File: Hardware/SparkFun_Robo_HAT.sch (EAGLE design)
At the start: 128 parts, among them J1 RASPBERRYPI-40-PIN-GPIO_PTH_R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, J11 EXT MTR PWR, J18 ISP, J2 CORTEX_DEBUGPTH, J20 USB C, J7 EXT SERVO PWR, J8 EXT 5V PWR, Q1 310mA/60V/1.6Ω, Q23 20V/0.2A/8MHz/1.2Ω/1Vth, Q24 20V/0.2A/8MHz/1.2Ω/1Vth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

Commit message: sch cleanup and drc stuff in brd
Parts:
- removed J2: CORTEX_DEBUGPTH, Pete_Connectors_Retired:CORTEX_DEBUGPTH
- removed TP18, TP19, TP24: TEST-POINTTP_15TH_THRU, SparkFun-Connectors:TEST-POINTTP_15TH_THRU
- added J23: CORTEX_JTAG_DEBUG_PTH, SparkFun-Connectors:CORTEX_JTAG_DEBUG_PTH
- added TP4, TP6: TEST-POINTTP_15TH_THRU, SparkFun-Connectors:TEST-POINTTP_15TH_THRU
- added TP9: TEST-POINT3, SparkFun-Connectors:TEST-POINT3
- TP5: value 1.8V -> TEST-POINTTP_15TH_THRU; device SparkFun-Connectors:TEST-POINT3 -> SparkFun-Connectors:TEST-POINTTP_15TH_THRU
- renumbered TP11 to TP7, TP12 to TP8
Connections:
- net !MTR_RST: now also J23.!RESET; no longer J2.NRESET
- net 1.8V: now also TP9.1; no longer TP5.1
- net 3.3V: now also J23.VCC; no longer J2.VCC
- net GND: now also J23.GND@3, J23.GND@5, J23.GNDDTCT, J23.KEY; no longer J2.GND@3, J2.GND@5, J2.GNDDTCT, J2.KEY
- net P3.2: now also J23.SWDIO/TMS; no longer J2.SWDIO/TMS
- net P3.3: now also J23.SWDCLK/TCK; no longer J2.SWDCLK/TCK
- net PI-5V: now also TP6.1; no longer TP24.1
- net SCL_3.3V: now also TP4.1; no longer TP18.1
- net SDA_3.3V: now also TP5.1; no longer TP19.1
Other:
- note added: "Servo Controller based on a design by Mike Hord Serial Controlled Motor Driver based on designs by Marshall Taylor, Alex Wende ICM-20948 based on a design by Owen Lyke ATTINY84 Encoder based on a design by Nathan Seidle"
- moved on the sheet: C12, C13, C14, C24, C25, J10, J19, J22, J3, J4, J5, U5

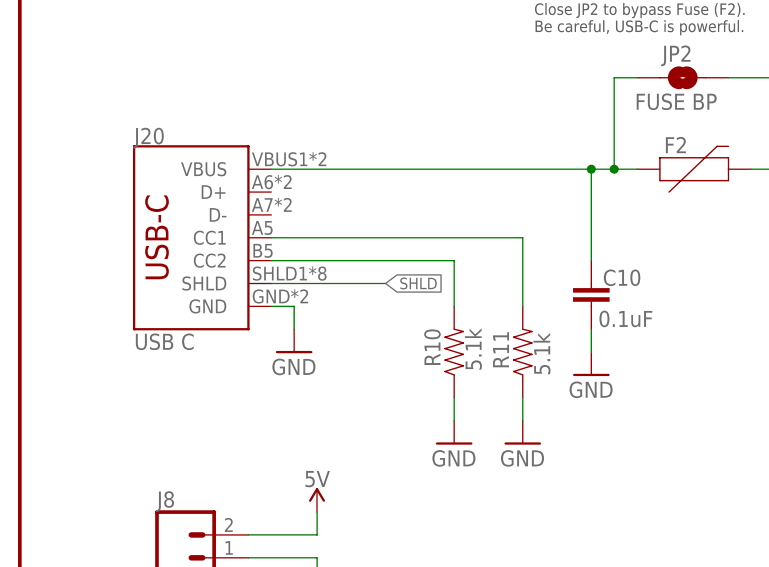
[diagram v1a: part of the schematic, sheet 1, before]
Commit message: removed USB C Shield polygon
to let more GND flow under connector up to Pi Header.
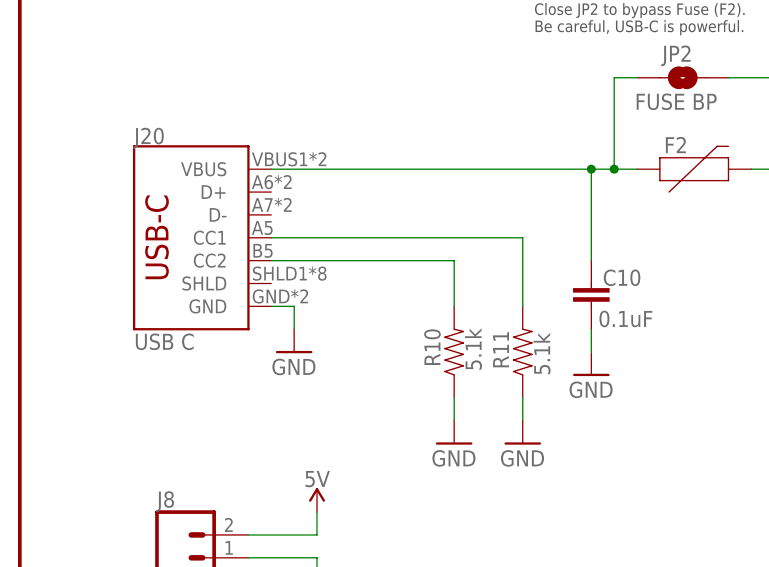
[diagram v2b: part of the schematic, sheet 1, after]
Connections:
- removed net SHLD: J20.SHLD
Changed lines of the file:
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@@
-</segment>
-</net>
-<net name="SHLD" class="0">
-<segment>
-<wire x1="27.94" y1="223.52" x2="40.64" y2="223.52" width="0.1524" layer="91"/>
-<label x="40.64" y="223.52" size="1.27" layer="95" font="vector" xref="yes"/>
-<pinref part="J20" gate="J1" pin="SHLD"/>
 </segment>
 </net>

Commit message: Engineer 1st run of checklist
added measures and SS path, cleaned up sch a bit more.
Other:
- note added: "VCC RANGE: 5V only (via USB or J8)"
- note removed: "VCC RANGE: 5V only (via USB or J21)"
- moved on the sheet: C11, C16, C2, C23, C26, C27, J18, JP13, R22, R37, R38, R39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

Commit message: post design review changes
-moved TP P3.0 programming pSoc onto grid
-Added pulldown resistor on Config line on PSoc
-Added trestric under pSoC to avoid GND pad nubbins.
-Added pullup resistors to SDA_OUT and SCL_OUT, as consistent with original serial controlled motor driver.
-Switched over to design block for pi header and slots. re-routed some stuff to make it work.
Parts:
- removed FD2, FD3, FD4: FIDUCIALUFIDUCIAL, SparkFun-Aesthetics:FIDUCIALUFIDUCIAL
- removed J1: RASPBERRYPI-40-PIN-GPIO_PTH_REFERENCE, SparkFun-Connectors:RASPBERRYPI-40-PIN-GPIO_PTH_REFERENCE
- added FD5, FD7, FD8: FIDUCIALUFIDUCIAL, SparkFun-Aesthetics:FIDUCIALUFIDUCIAL
- added H10, H11, H12, H9: STAND-OFFTIGHT, SparkFun-Hardware:STAND-OFFTIGHT
- added J2: RASPBERRYPI-40-PIN-GPIO_PTH_NO_SHROUD, SparkFun-Connectors:RASPBERRYPI-40-PIN-GPIO_PTH_NO_SHROUD
- added R12, R3, R6: 5.1k, SparkFun-Resistors:5.1KOHM5.1KOHM-0603-1/10W-1%
- renumbered FD1 to FD6
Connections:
- new net CONFIG_OUT: R6.2, U6G4.P3.0
- new net SCL_OUT: R12.1, U6G5.P4.0
- new net SDA_OUT: R3.1, U6G5.P4.1
- net !ENC_INT: now also J2.GP4; no longer J1.GP4
- net 3.3V: now also J2.3.3V, R12.2, R3.2; no longer J1.3.3V
- net GND: now also J2.GND, R6.1; no longer J1.GND
- net IMU_INT_3.3V: now also J2.CE1; no longer J1.CE1
- net N$20: now also J2.5V; no longer J1.5V
- net SCL_3.3V: now also J2.SCL; no longer J1.SCL
- net SDA_3.3V: now also J2.SDA; no longer J1.SDA
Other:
- moved on the sheet: C17, C18, C19, C20, C21, C22, C23, R25, R26, U6G1, U6G3, U6G4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

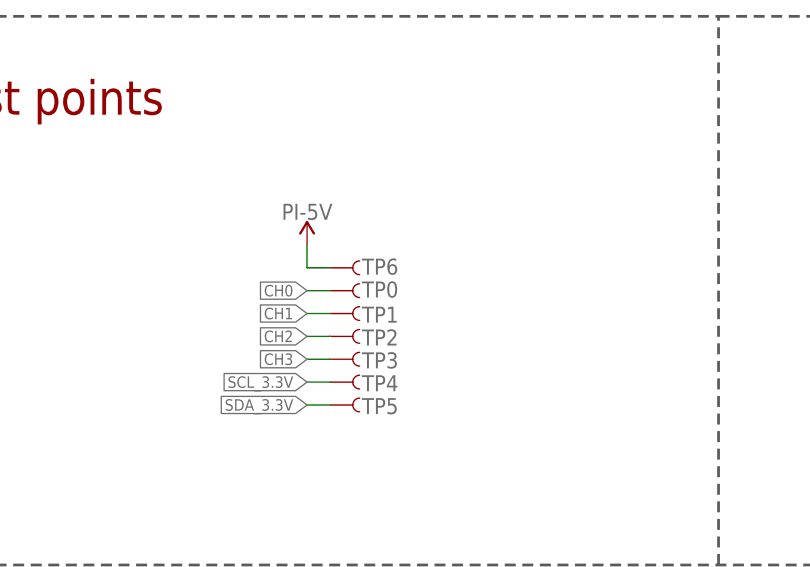
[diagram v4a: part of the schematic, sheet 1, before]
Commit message: post double-check changes - ready for proto v01
-moved TP6 to SMT pad style and on grid
-updated tran-14386 (ideal diode) to have polarity mark outside package
-nudged vias to avoid silk labels
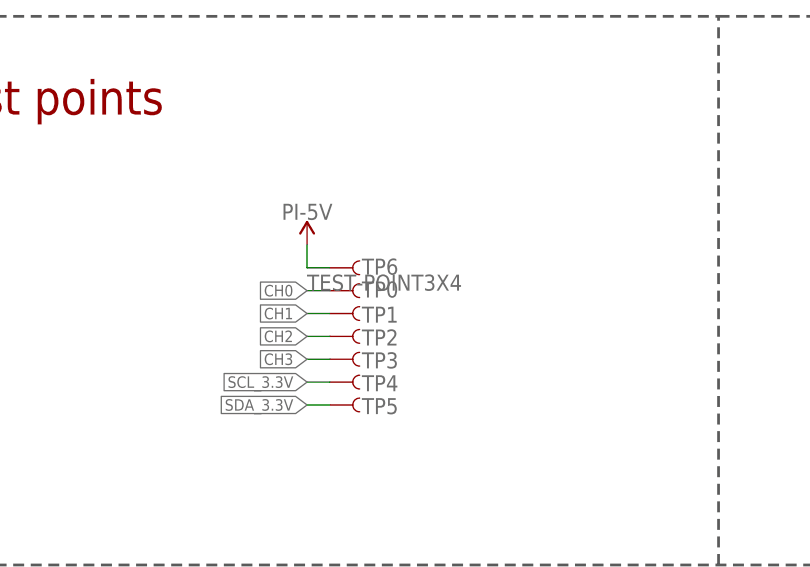
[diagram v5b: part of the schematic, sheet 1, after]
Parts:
- Q23, Q24, Q27, Q28: device SparkFun-DiscreteSemi:MOSFET-NCH-RE1C002UN -> SparkFun-DiscreteSemi:MOSFET-NCH-RE1C00UNTL
- TP6: value TEST-POINTTP_15TH_THRU -> TEST-POINT3X4; device SparkFun-Connectors:TEST-POINTTP_15TH_THRU -> SparkFun-Connectors:TEST-POINT3X4

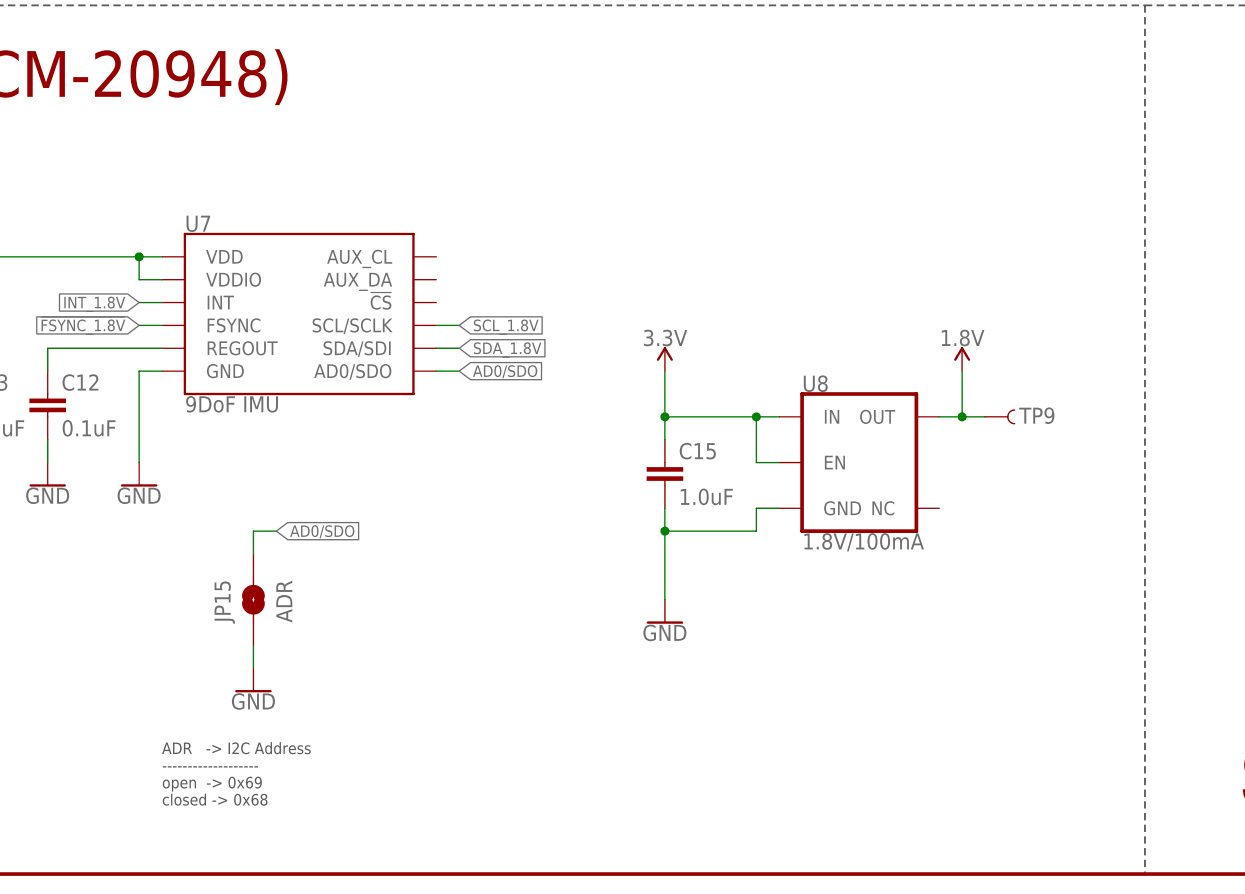
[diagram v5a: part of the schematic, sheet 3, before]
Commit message: Connected IMU CS pin to 1.8V, Added IMU ADR PU 2.2K resistor
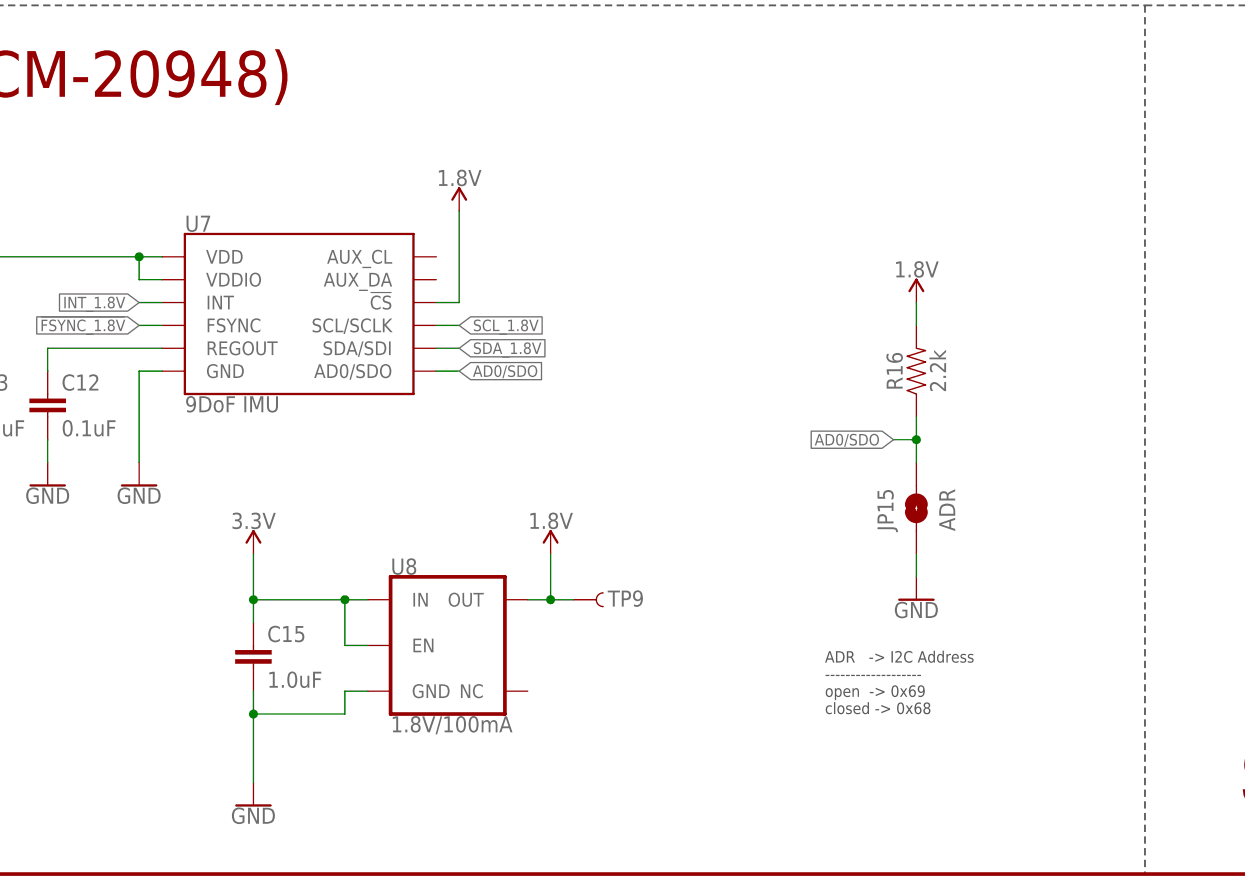
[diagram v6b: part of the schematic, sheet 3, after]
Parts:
- added R16: 2.2k, SparkFun-Resistors:2.2KOHM-0402T-1/16W-1%
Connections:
- net 1.8V: now also R16.2, U7.!CS
- net AD0/SDO: now also R16.1
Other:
- moved on the sheet: C15, JP15, TP9, U8

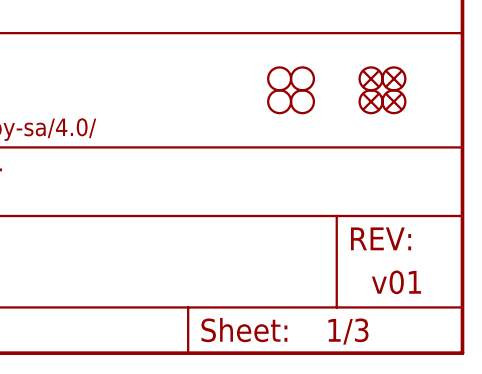
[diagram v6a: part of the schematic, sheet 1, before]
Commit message: bumped version to v10 in sch and brd
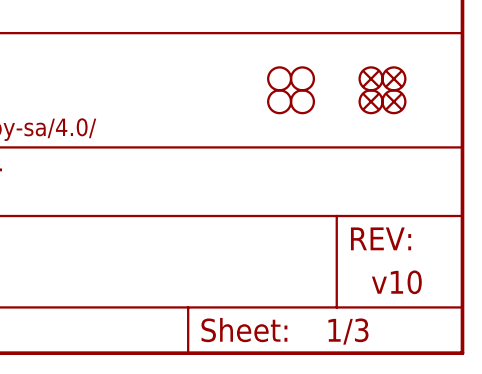
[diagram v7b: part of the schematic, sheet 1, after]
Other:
- note added: "v10"
- note removed: "v01"
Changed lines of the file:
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@@
 <plain>
 <text x="349.758" y="11.43" size="2.54" layer="94" font="vector">Pete Lewis</text>
-<text x="421.64" y="6.604" size="2.54" layer="94" font="vector" ratio="12">v01</text>
+<text x="421.64" y="6.604" size="2.54" layer="94" font="vector" ratio="12">v10</text>
 <wire x1="139.7" y1="152.4" x2="139.7" y2="91.44" width="0.3048" layer="97" style="longdash"/>
 <wire x1="139.7" y1="91.44" x2="139.7" y2="0" width="0.3048" layer="97" style="longdash"/>
@@
 <text x="166.624" y="11.43" size="2.54" layer="94" font="vector">Pete Lewis</text>
 <text x="5.08" y="177.8" size="3.81" layer="94" font="vector">Motor Driver IC - PSoC I/O</text>
-<text x="237.49" y="7.62" size="2.54" layer="94" font="vector">v01</text>
+<text x="237.49" y="7.62" size="2.54" layer="94" font="vector">v10</text>
 <text x="123.698" y="18.288" size="1.27" layer="97" font="vector" rot="MR180">P3.2 swd_io[0]
 P3.3 swd_clk[0]
@@
 <text x="261.874" y="11.176" size="1.778" layer="97" font="vector">*For frame synchronization support
 (3.3V Logic level)</text>
-<text x="421.386" y="7.366" size="2.54" layer="94" font="vector">v01</text>
+<text x="421.386" y="7.366" size="2.54" layer="94" font="vector">v10</text>
 <text x="349.758" y="11.43" size="2.54" layer="94" font="vector">Pete Lewis</text>
 </plain>

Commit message: moving to SMD stackable solution... 99 done
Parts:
- J19: value (none) -> QWIIC_RIGHT_ANGLE
- J2: value RASPBERRYPI-40-PIN-GPIO_PTH_NO_SHROUD -> RASPBERRYPI-40-PIN-GPIO_SMD_STACKABLE; device SparkFun-Connectors:RASPBERRYPI-40-PIN-GPIO_PTH_NO_SHROUD -> SparkFun-Connectors:RASPBERRYPI-40-PIN-GPIO_SMD_STACKABLE
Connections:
- new net CE0: J2.CE0
- new net GP12: J2.GP12
- new net GP13: J2.GP13
- new net GP16: J2.GP16
- new net GP17: J2.GP17
- new net GP18: J2.GP18#
- new net GP19: J2.GP19
- new net GP20: J2.GP20
- new net GP21: J2.GP21
- new net GP22: J2.GP22
- new net GP23: J2.GP23
- new net GP24: J2.GP24
- new net GP25: J2.GP25
- new net GP26: J2.GP26
- new net GP27: J2.GP27
- new net GP5: J2.GP5
- new net GP6: J2.GP6
- new net ID_SC: J2.ID_SC
- new net ID_SD: J2.ID_SD
- new net PI_MISO: J2.MISO
- new net PI_MOSI: J2.MOSI
- new net PI_RXI: J2.RXI
- new net PI_TXO: J2.TXO
- new net SCLK: J2.SCLK
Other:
- moved on the sheet: J2
